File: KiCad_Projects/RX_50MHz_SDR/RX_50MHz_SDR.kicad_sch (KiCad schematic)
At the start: 3 parts, among them U1 ESP32-S3, U2 Mixer, U3 LNA

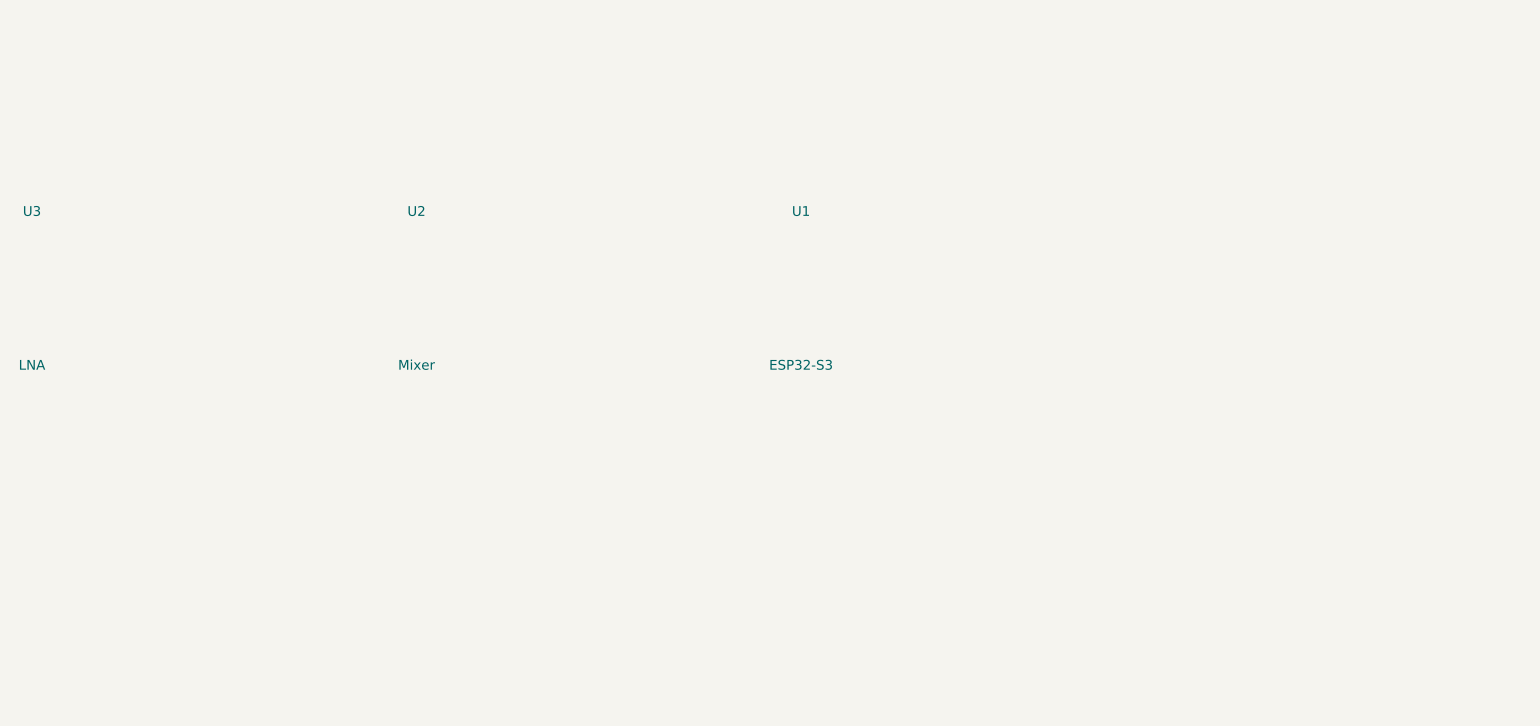
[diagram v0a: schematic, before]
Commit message: Add SPF5043Z datasheet to repository
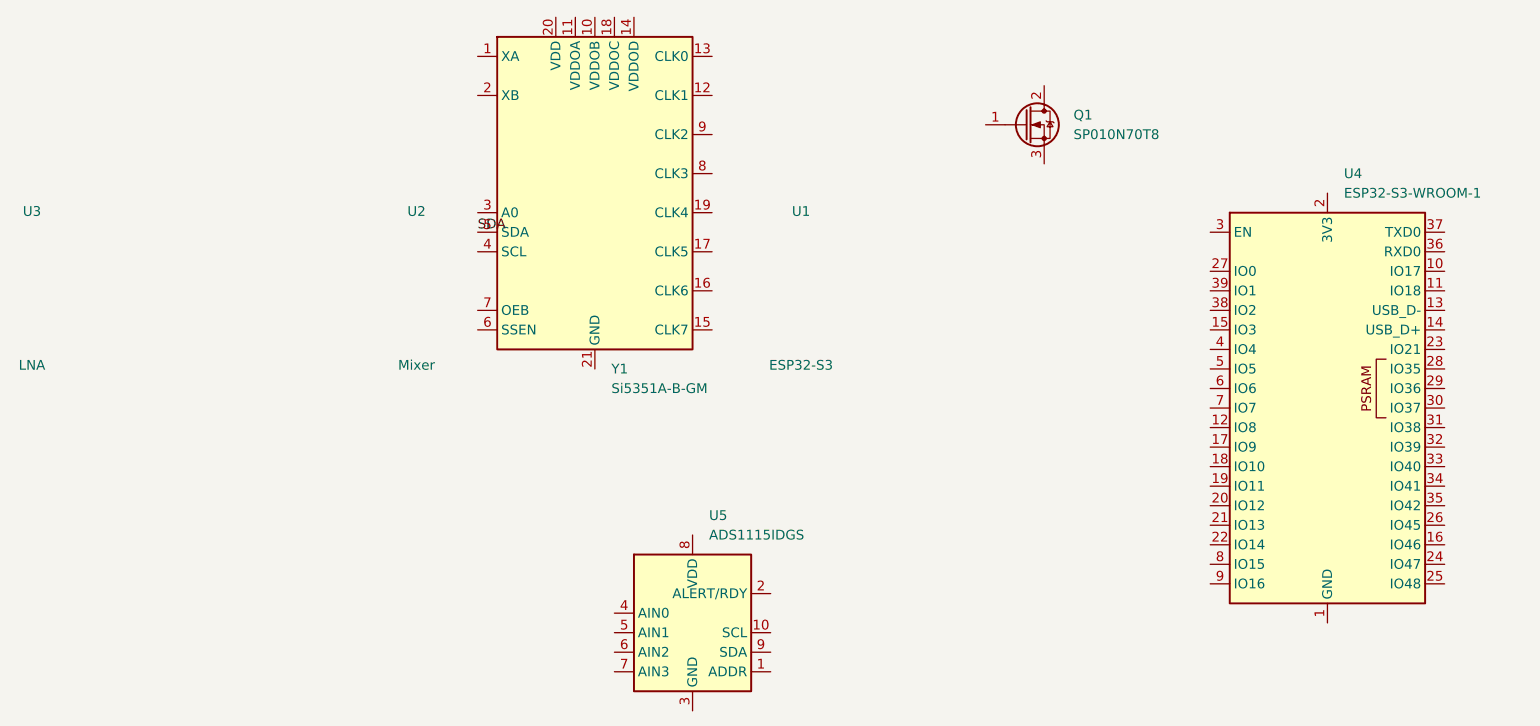
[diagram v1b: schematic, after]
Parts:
- added Q1: SP010N70T8, Package_TO_SOT_SMD:SOT-89-3, symbol Transistor_FET_Other:SP010N70T8
- added U4: ESP32-S3-WROOM-1, RF_Module:ESP32-S3-WROOM-1, symbol RF_Module:ESP32-S3-WROOM-1
- added U5: ADS1115IDGS, Package_SO:TSSOP-10_3x3mm_P0.5mm, symbol Analog_ADC:ADS1115IDGS
- added Y1: Si5351A-B-GM, Package_DFN_QFN:QFN-20-1EP_4x4mm_P0.5mm_EP2.7x2.7mm, symbol Oscillator:Si5351A-B-GM
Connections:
- new net: U4.1 (GND), U4.40 (GND), U4.41 (GND)
- new net SDA: Y1.5 (SDA)
